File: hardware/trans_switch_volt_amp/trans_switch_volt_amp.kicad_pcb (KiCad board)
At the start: 2 copper layers, 167.4 x 55.9 mm, 19 parts, among them J1 to biopac, J2 To biopac, Q1 BC182L_NPN, Q2 BC182L_NPN, U1 LM741, U2 LM741

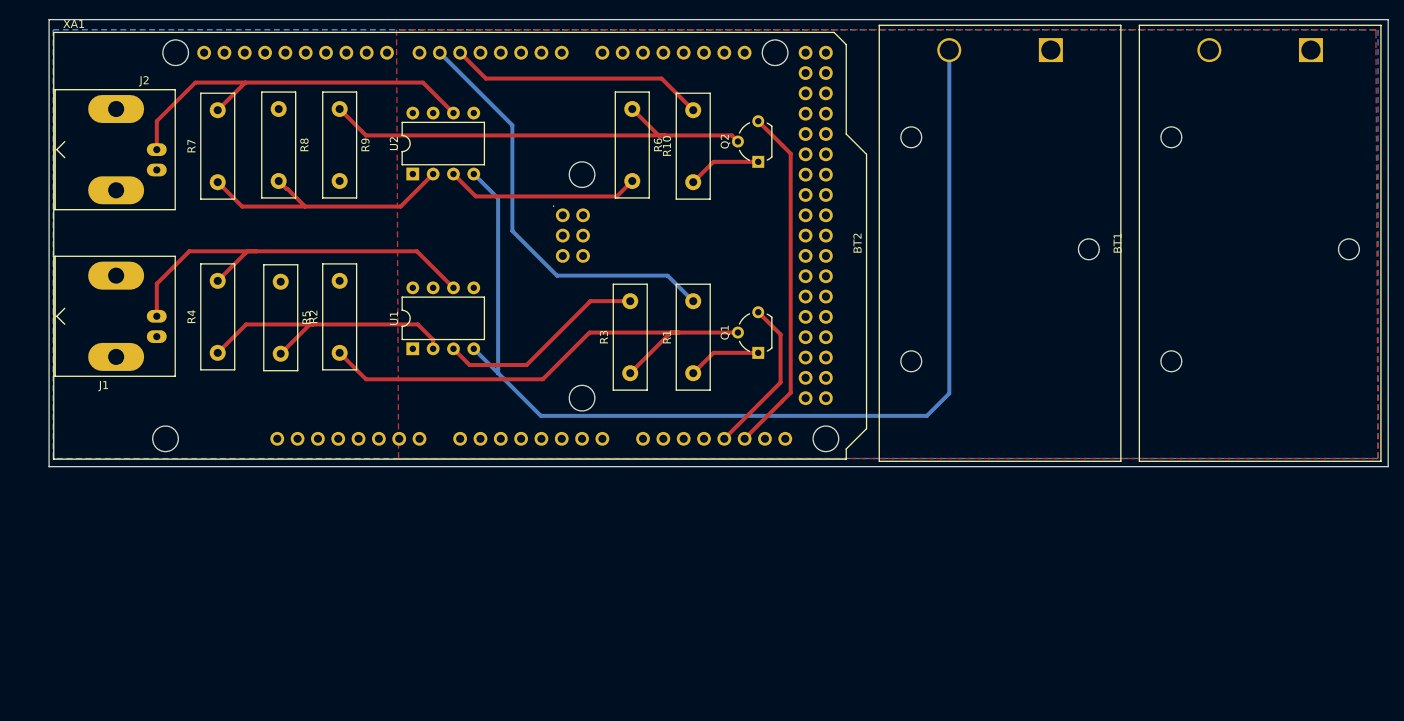
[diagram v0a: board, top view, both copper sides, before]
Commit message: finish writing warnings and lincenses on the board
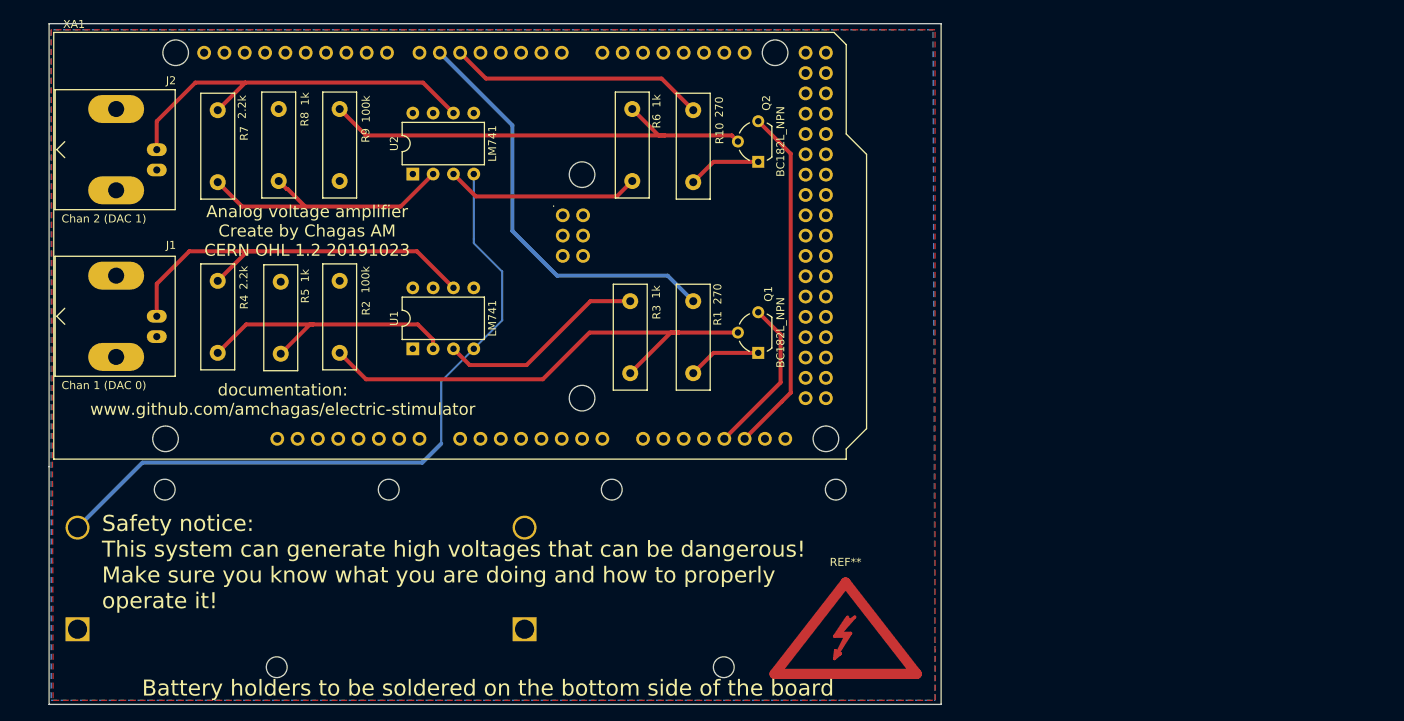
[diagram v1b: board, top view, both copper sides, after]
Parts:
- added REF**: Symbol_Highvoltage_Type2_CopperTop_Small, Symbol:Symbol_Highvoltage_Type2_CopperTop_Small, F.Cu at (179.1, 142.5)
- BT1, BT2: value Battery_Cell -> 9V Battery; moved to B.Cu
- J1: value to biopac -> Chan 1 (DAC 0)
- J2: value To biopac -> Chan 2 (DAC 1)
- moved BT2 141.6 mm to (83.1, 140.7), turned to 180 degrees
- moved BT1 122.1 mm to (138.9, 140.7), turned to 180 degrees
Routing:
- net Net-(BT2-Pad2): track 133.1 -> 88.1 mm
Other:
- board size 167.4 x 55.9 mm -> 111.5 x 85.1 mm
- board text added: "Analog voltage amplifier Create by Chagas AM CERN OHL 1.2 20191023"
- board text added: "Battery holders to be soldered on the bottom side of the board"
- board text added: "Safety notice: This system can generate high voltages that can be dangerous! Make sure you know what you are doing and how to properly operate it!"
- board text added: "documentation: www.github.com/amchagas/electric-stimulator"

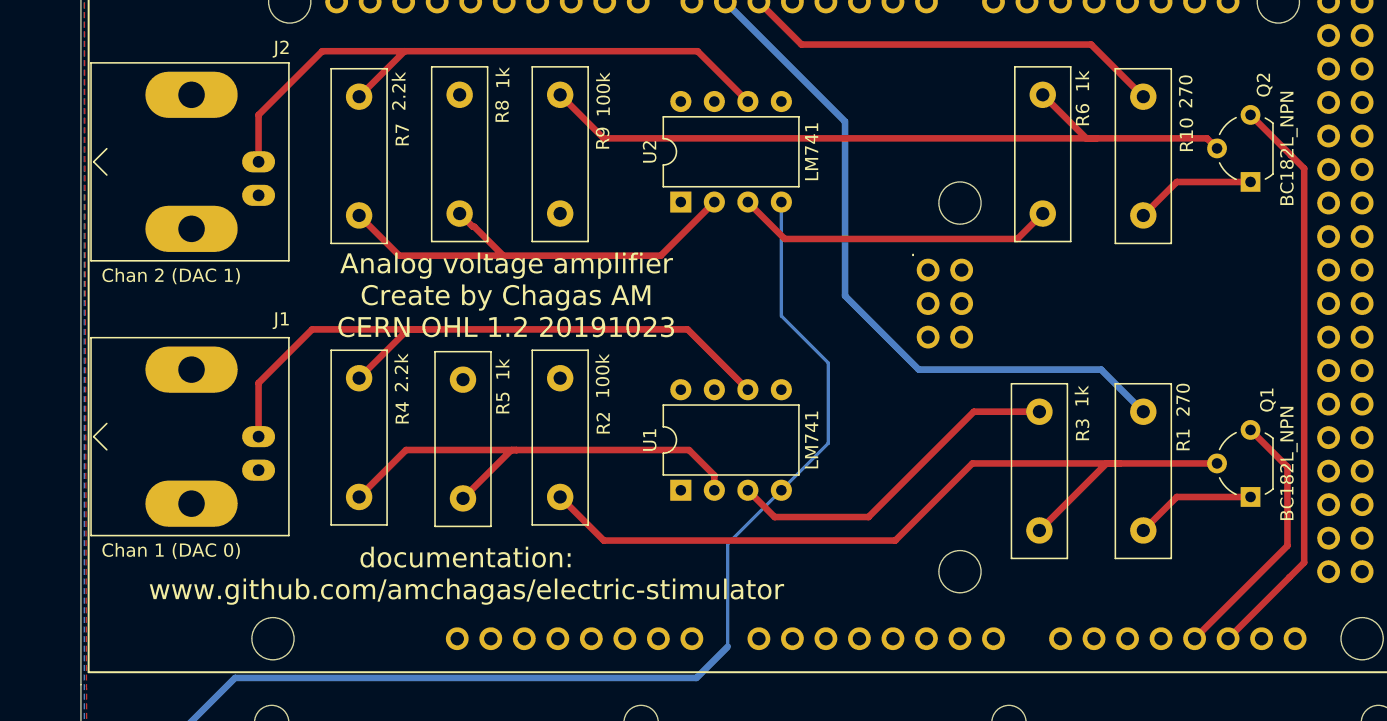
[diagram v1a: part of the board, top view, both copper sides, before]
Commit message: update board and fixed transistor bug
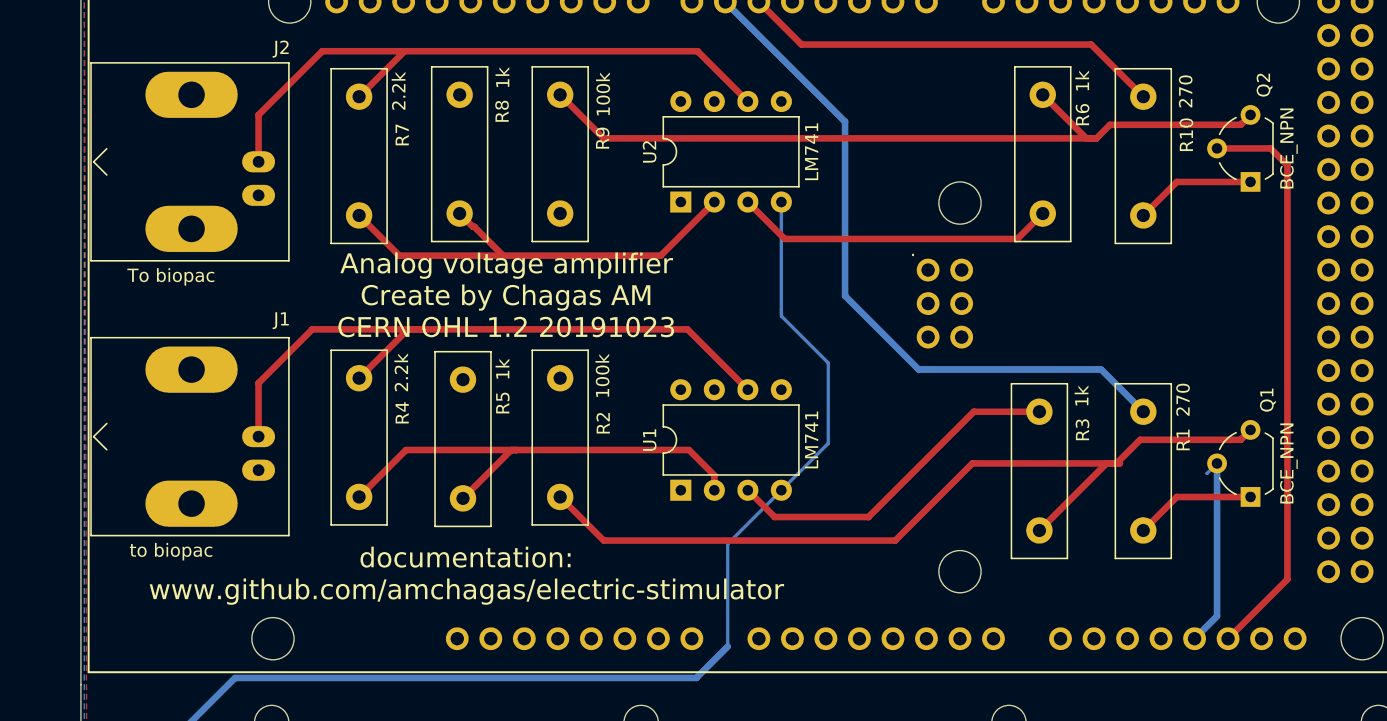
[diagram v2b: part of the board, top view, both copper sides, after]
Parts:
- BT1, BT2: value 9V Battery -> Battery_Cell
- J1: value Chan 1 (DAC 0) -> to biopac
- J2: value Chan 2 (DAC 1) -> To biopac
- Q1, Q2: value BC182L_NPN -> BCE_NPN
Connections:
- R2 pad 1: Net-(Q1-Pad2) -> Net-(Q1-Pad3)
- R3 pad 1: Net-(Q1-Pad2) -> Net-(Q1-Pad3)
- R6 pad 1: Net-(Q2-Pad2) -> Net-(Q2-Pad3)
- R9 pad 1: Net-(Q2-Pad2) -> Net-(Q2-Pad3)
- XA1 pad DAC0: Net-(Q1-Pad3) -> Net-(Q1-Pad2)
- XA1 pad DAC1: Net-(Q2-Pad3) -> Net-(Q2-Pad2)
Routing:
- net Net-(Q1-Pad2): track 61.8 -> 15.1 mm
- net Net-(Q1-Pad3): track 19.9 -> 65.6 mm
- net Net-(Q2-Pad3): track 43.8 -> 59.9 mm
- net Net-(Q2-Pad2): track 56.9 -> 43.6 mm
